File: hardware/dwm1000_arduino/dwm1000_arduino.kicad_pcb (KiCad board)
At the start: 2 copper layers, 66 x 76.2 mm, 29 parts, among them J1 RAW_PWR, J2 PWR_IN, J3 UART, J4 SPI, J5 NEO_OUT, J6 DEBUG

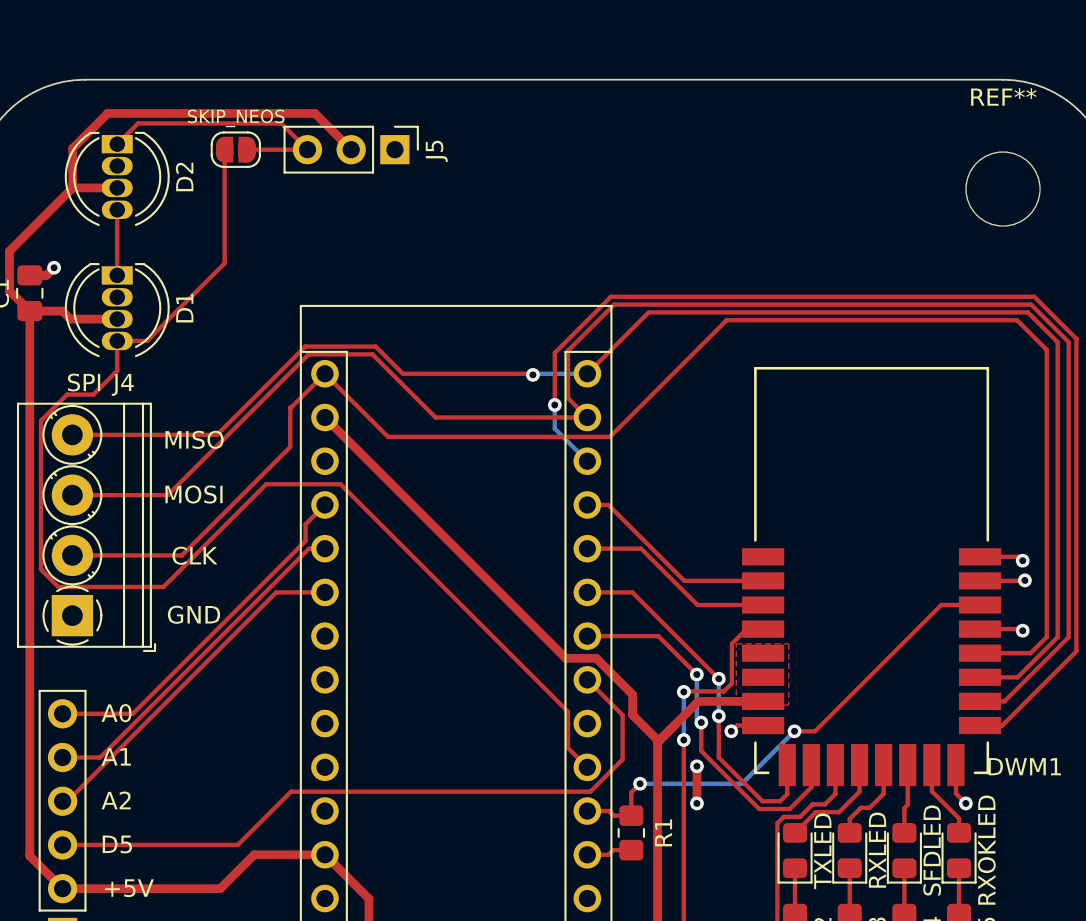
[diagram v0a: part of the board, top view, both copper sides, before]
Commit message: fix ground plane, fix connector placement, add silkscreen
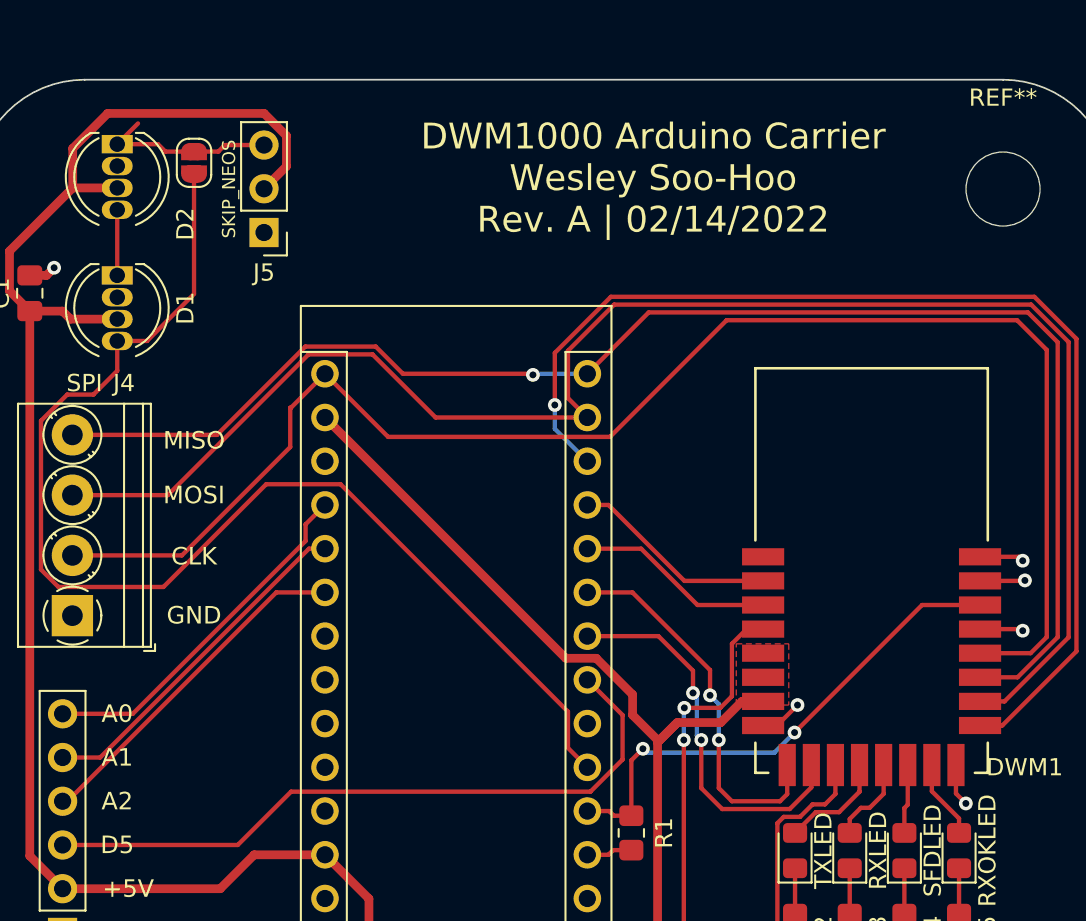
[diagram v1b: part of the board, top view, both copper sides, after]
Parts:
- moved J5 9.00 mm to (128.5, 63.5), turned to 180 degrees
- moved JP1 2.54 mm to (124.5, 59.4), turned to 90 degrees
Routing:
- net NEO_OUT: track 15.7 -> 10.6 mm
- net NEO_DATA: track 73.4 -> 71.2 mm
- net GND: track 25.2 -> 23.6 mm, vias 12 -> 10
- net /MCUs/DWM_IRQ: track 28.8 -> 30.1 mm
- net /MCUs/DWM_SPIPOL: track 21.4 -> 22.7 mm
- net /MCUs/DWM_SPIHA: track 21.2 -> 22.2 mm
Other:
- board text added: "DWM1000 Arduino Carrier Wesley Soo-Hoo Rev. A | 02/14/2022"
